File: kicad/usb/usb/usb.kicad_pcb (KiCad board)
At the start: 2 copper layers, 31 x 27 mm, 19 parts, among them J1 USB_C_Receptacle_USB2.0_14P, J2 PH2.0mm 2P, J3 Conn_01x07_Pin, Q1 BSS84, SW1 PWR, U1 S-T111B33MC-OGSTFU, U2 MCP73831-2-OT

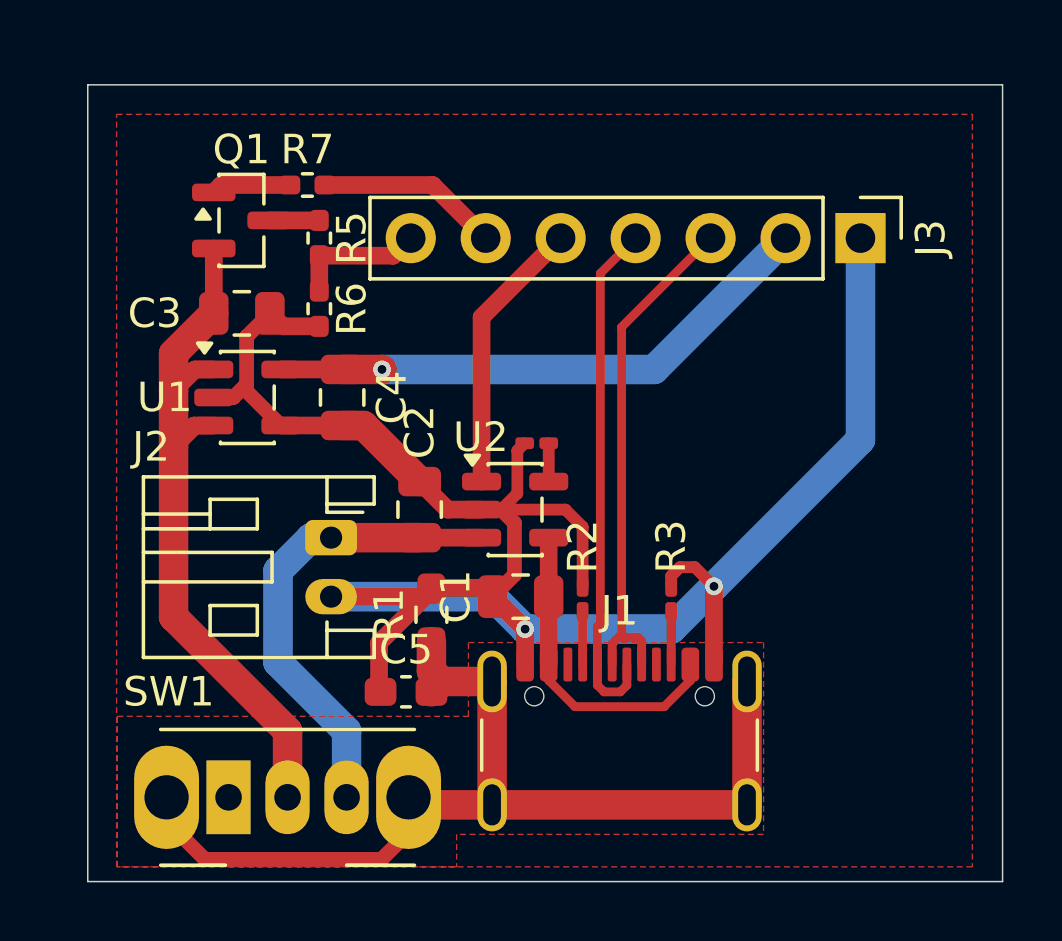
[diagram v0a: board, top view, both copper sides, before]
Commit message: Added pulldown resistor, made vsense enable always on
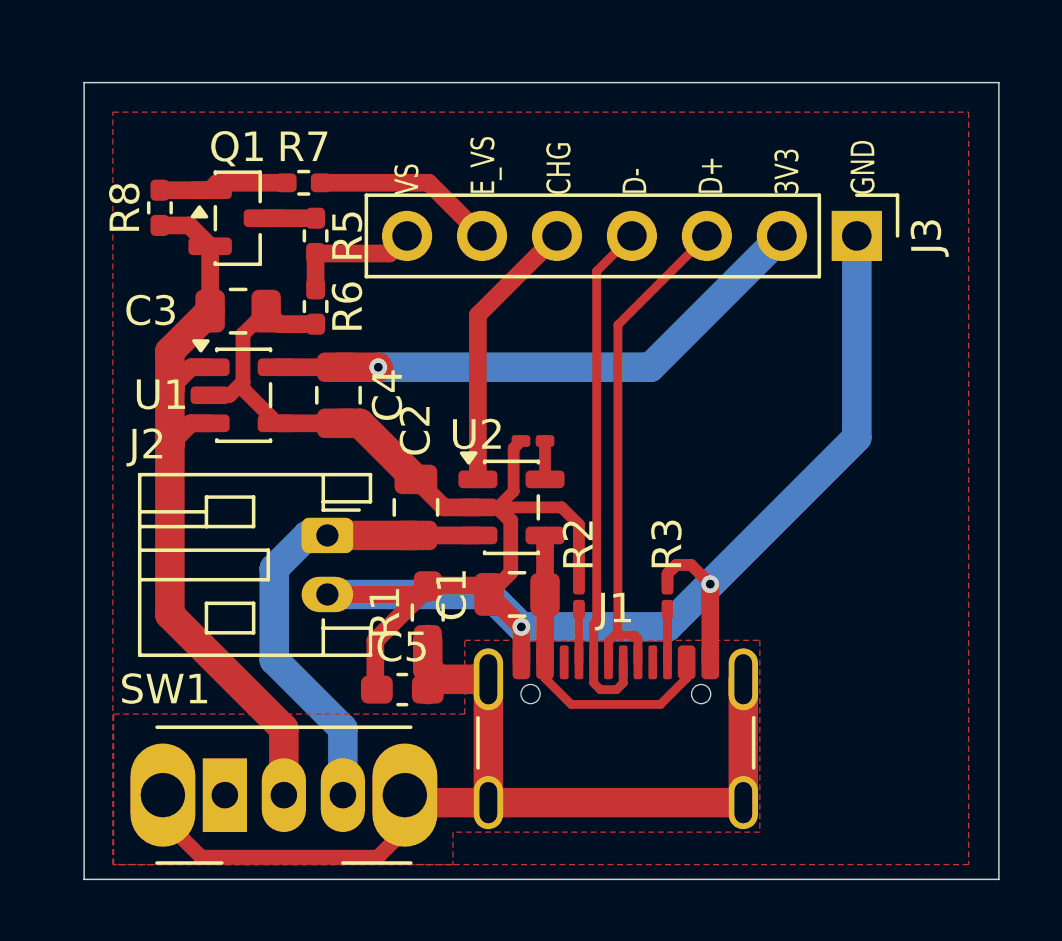
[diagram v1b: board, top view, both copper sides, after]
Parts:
- added R8: 1m, Resistor_SMD:R_0402_1005Metric_Pad0.72x0.64mm_HandSolder, F.Cu at (82.5, 91.6)
- moved C1 0.15 mm to (94.6, 104.7)
- moved C2 0.15 mm to (91.2, 101.8)
- moved C3 0.15 mm to (85.2, 95.1)
- moved C4 0.15 mm to (88.5, 98.0)
- moved C5 0.15 mm to (90.7, 107.9)
- moved J2 0.15 mm to (88.2, 102.7)
- moved J3 0.15 mm to (106.1, 92.5)
- moved Q1 0.15 mm to (85.1, 92.0)
- moved R1 0.15 mm to (91.6, 105.3)
- moved R2 0.15 mm to (96.7, 104.8)
- moved R3 0.15 mm to (99.7, 104.8)
- moved R4 0.15 mm to (95.1, 99.5)
- moved R5 0.15 mm to (87.8, 92.5)
- moved R6 0.15 mm to (87.8, 94.9)
- moved R7 0.15 mm to (87.4, 90.8)
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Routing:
- net VSENSE: track 24.1 -> 26.1 mm
- net Net-(Q1-G): track 2.68 -> 4.38 mm
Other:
- board text added: "VS E_VS CHG D- D+ 3V3 GND"

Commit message: Swapped the p-channel mosfet for a pnp transistor
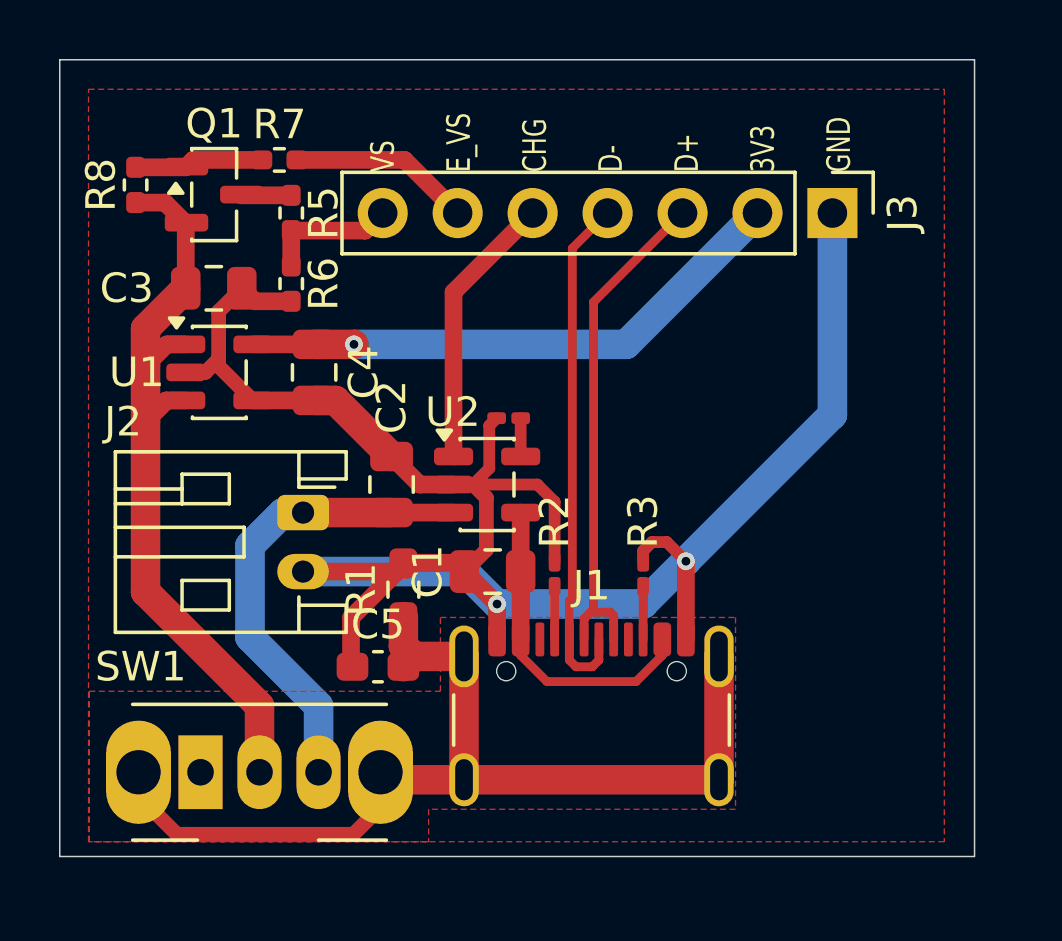
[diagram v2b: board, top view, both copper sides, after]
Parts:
- Q1: value BSS84 -> MMBT3906
- moved C2 1.13 mm to (90.3, 101.0)
- moved C4 1.13 mm to (87.7, 97.2)
- moved J1 1.13 mm to (97.1, 109.9)
- moved J2 1.13 mm to (87.3, 101.9)
- moved R1 1.13 mm to (90.8, 104.5)
- moved R2 1.13 mm to (95.9, 104.0)
- moved R3 1.13 mm to (98.9, 104.0)
- moved R4 1.13 mm to (94.3, 98.7)
- moved R5 1.13 mm to (87.0, 91.8)
- moved R7 1.13 mm to (86.5, 90.0)
- moved SW1 1.13 mm to (83.9, 110.7)
- moved U1 1.13 mm to (84.5, 97.2)
- moved C3 1.13 mm to (84.3, 94.3)
- moved C5 1.13 mm to (89.9, 107.2)
- moved R6 1.13 mm to (87.0, 94.2)
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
